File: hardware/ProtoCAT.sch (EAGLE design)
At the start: 46 parts, among them U1 ARDUINO, U3 TB6621FNG

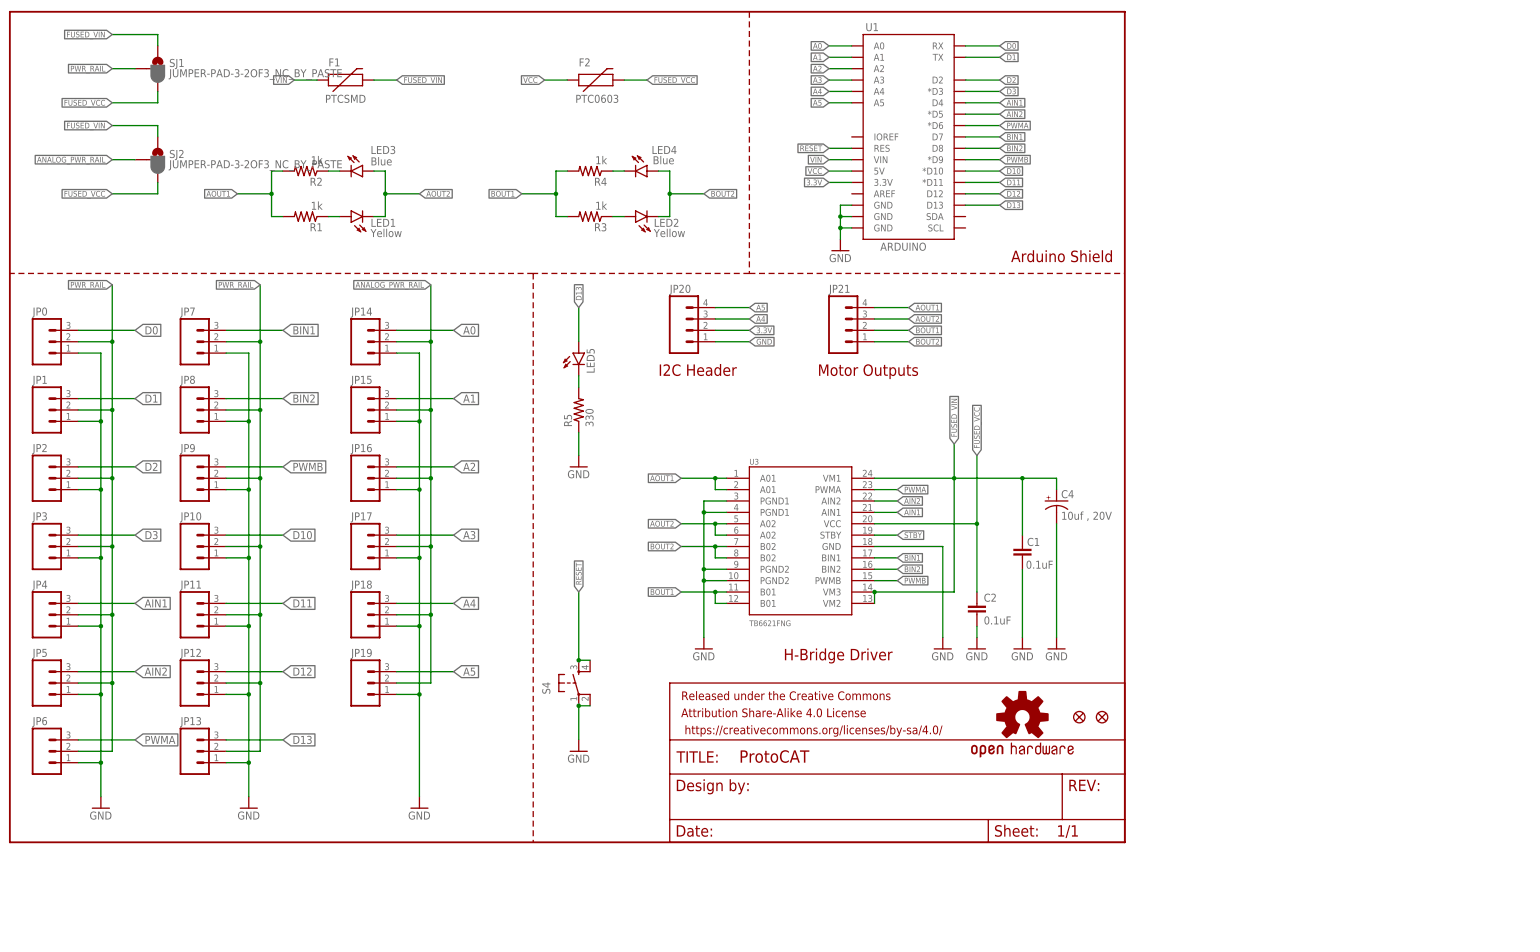
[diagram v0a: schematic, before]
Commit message: Updates per - engineering review mtg 8/18
added prototyping area
added cut/solder jumpers for A4/A5 SDA/SCL lines for Leo
added ~PWM labels on pins 3, 5, 6, 9, 10, 11
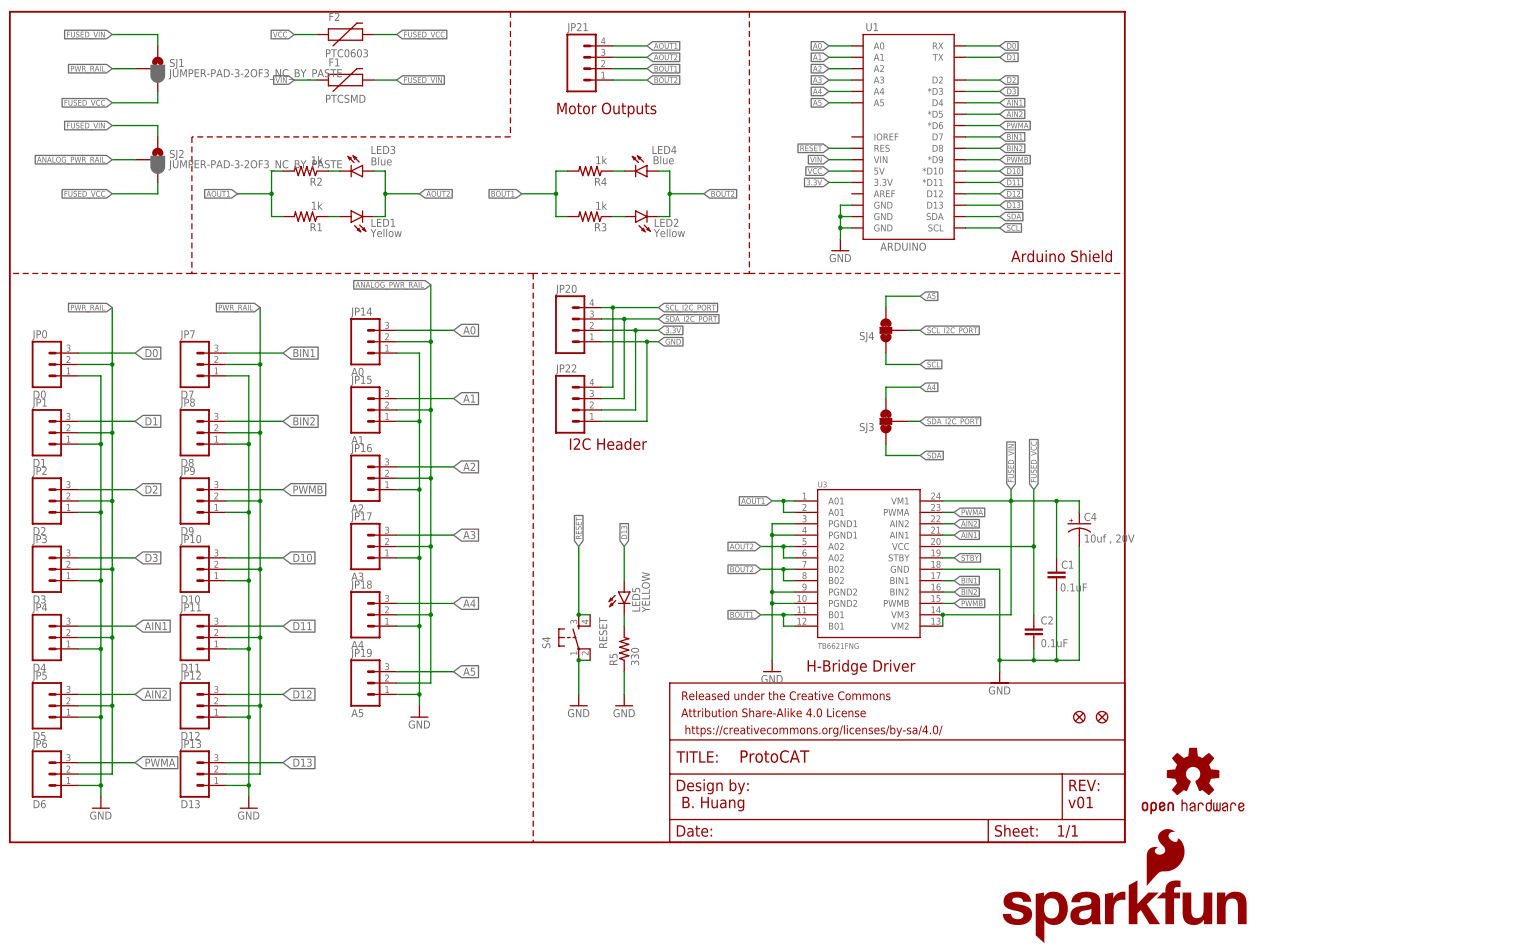
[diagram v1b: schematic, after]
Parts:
- added JP22: (no value), SparkFun-Connectors:M04PTH
- added LOGO2: SFE_LOGO_NAME_FLAME.1_INCH, SparkFun-Aesthetics:SFE_LOGO_NAME_FLAME.1_INCH
- added SJ3, SJ4: (no value), SparkFun-Passives:JUMPER-PAD-3-NC_BY_TRACE
- JP0: value (none) -> D0
- JP1: value (none) -> D1
- JP10: value (none) -> D10
- JP11: value (none) -> D11
- JP12: value (none) -> D12
- JP13: value (none) -> D13
- JP14: value (none) -> A0
- JP15: value (none) -> A1
- JP16: value (none) -> A2
- JP17: value (none) -> A3
- JP18: value (none) -> A4
- JP19: value (none) -> A5
- JP2: value (none) -> D2
- JP3: value (none) -> D3
- JP4: value (none) -> D4
- JP5: value (none) -> D5
- JP6: value (none) -> D6
- JP7: value (none) -> D7
- JP8: value (none) -> D8
- JP9: value (none) -> D9
- LED5: value (none) -> YELLOW
- S4: value (none) -> RESET
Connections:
- new net SCL: SJ4.1, U1.SCL
- new net SCL_I2C_PORT: JP20.4, JP22.4, SJ4.2
- new net SDA: SJ3.1, U1.SDA
- new net SDA_I2C_PORT: JP20.3, JP22.3, SJ3.2
- net 3.3V: now also JP22.2
- net A4: now also SJ3.3; no longer JP20.3
- net A5: now also SJ4.3; no longer JP20.4
- net GND: now also JP22.1
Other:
- note added: "B. Huang"
- note added: "v01"
- moved on the sheet: C1, C2, C4, F2, JP0, JP1, JP10, JP11, JP12, JP13, JP2, JP20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

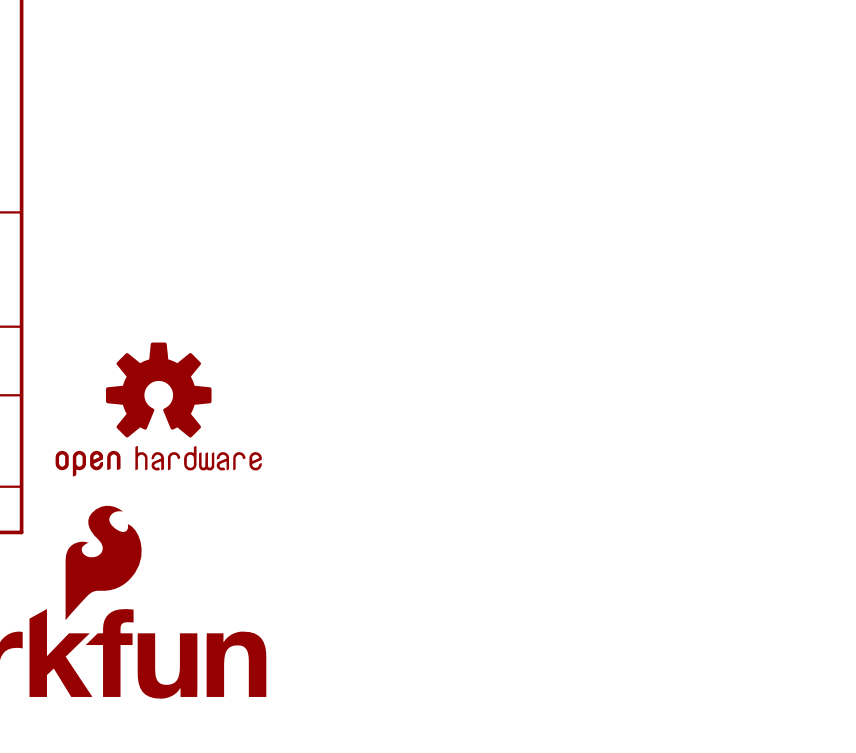
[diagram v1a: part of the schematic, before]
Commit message: Updated a few aesthetic elements on bottom side
Included Ludus and sparkfun logo on bottom layer
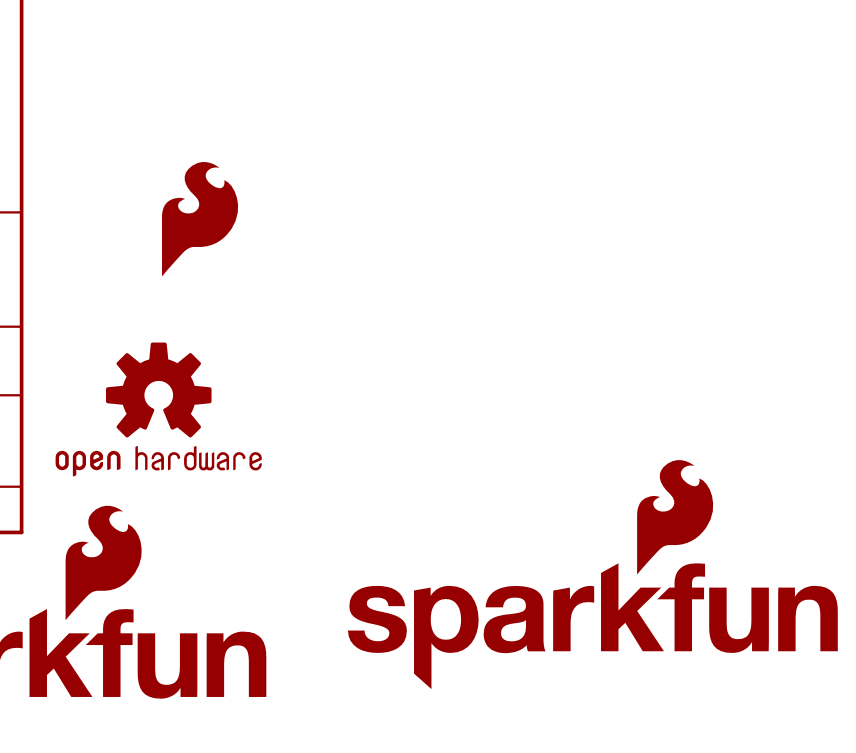
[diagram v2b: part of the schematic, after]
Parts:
- added LOGO3: SFE_LOGO_FLAME.2COP, SparkFun-Aesthetics:SFE_LOGO_FLAME.2COP
- added LOGO4: SFE_LOGO_NAME_FLAME.1_INCH, SparkFun-Aesthetics:SFE_LOGO_NAME_FLAME.1_INCH
- added U$1: SFE_LUDUS, SparkFun-Aesthetics:SFE_LUDUS
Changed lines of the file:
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@@
 <part name="SJ3" library="SparkFun-Passives" deviceset="JUMPER-PAD-3-NC_BY_TRACE" device=""/>
 <part name="SJ4" library="SparkFun-Passives" deviceset="JUMPER-PAD-3-NC_BY_TRACE" device=""/>
+<part name="U$1" library="SparkFun-Aesthetics" deviceset="SFE_LUDUS" device=""/>
+<part name="LOGO3" library="SparkFun-Aesthetics" deviceset="SFE_LOGO_FLAME" device=".2COP"/>
+<part name="LOGO4" library="SparkFun-Aesthetics" deviceset="SFE_LOGO_NAME_FLAME" device=".1_INCH" value="SFE_LOGO_NAME_FLAME.1_INCH"/>
 </parts>
 <sheets>
@@
 <instance part="SJ3" gate="G$1" x="195.58" y="93.98" rot="R180"/>
 <instance part="SJ4" gate="G$1" x="195.58" y="114.3" rot="R180"/>
+<instance part="U$1" gate="G$1" x="257.191559375" y="32.335265625" rot="R90"/>
+<instance part="LOGO3" gate="G$1" x="264.16" y="27.94"/>
+<instance part="LOGO4" gate="G$1" x="284.48" y="-17.78"/>
 </instances>
 <busses>
